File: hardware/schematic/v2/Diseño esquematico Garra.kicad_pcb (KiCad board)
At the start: 2 copper layers, 18 parts

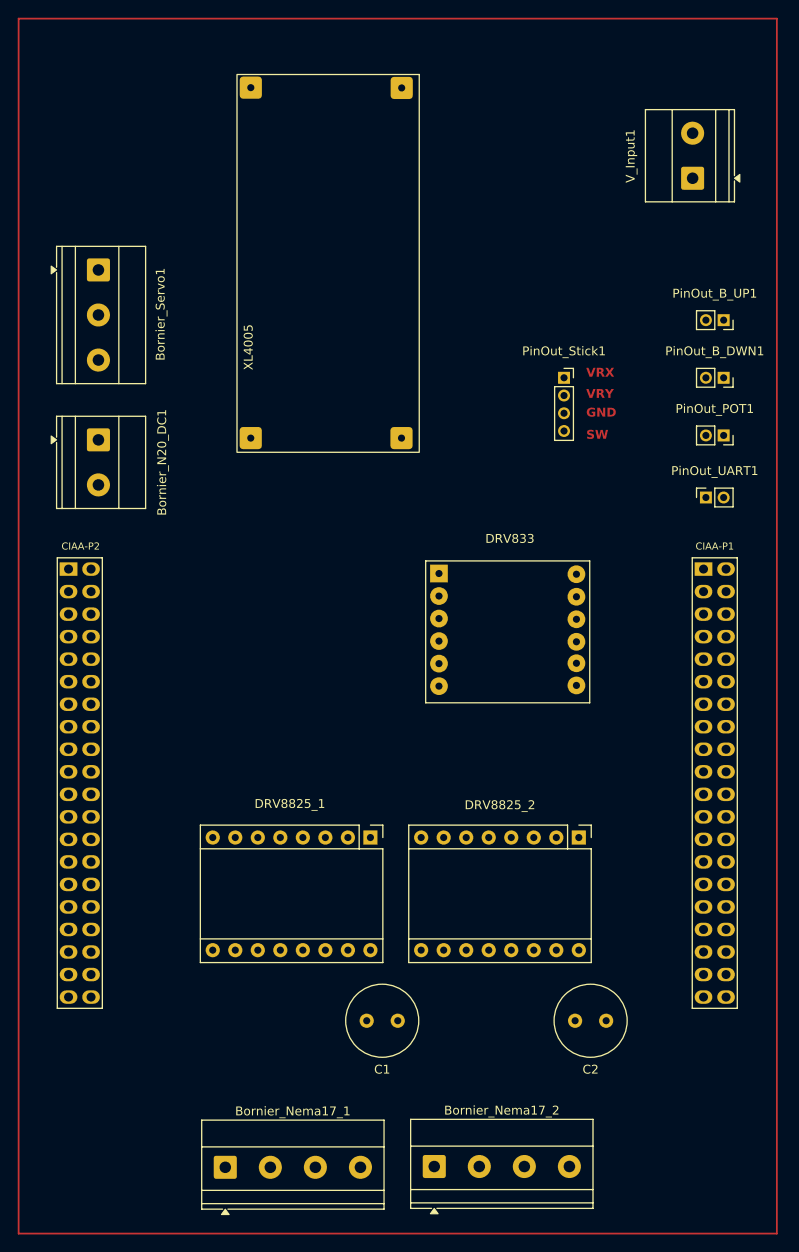
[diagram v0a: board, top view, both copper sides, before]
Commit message: feat: add PCB layout (#7)
* refactor

* feat: PCB routing first stage completed

* docs: Schematics PDF added

* fix: PCB border colision

* feat: Copper layers added to the PCB

* feat: New PCB design with new components [LED, B_M]

* feat: add through holes for connectivity & GNDs links

* feat: hole diameter adjustment

* fix: PDF

---------

Co-authored-by: ManuSavenia <saveniamanuel@egmail.com>
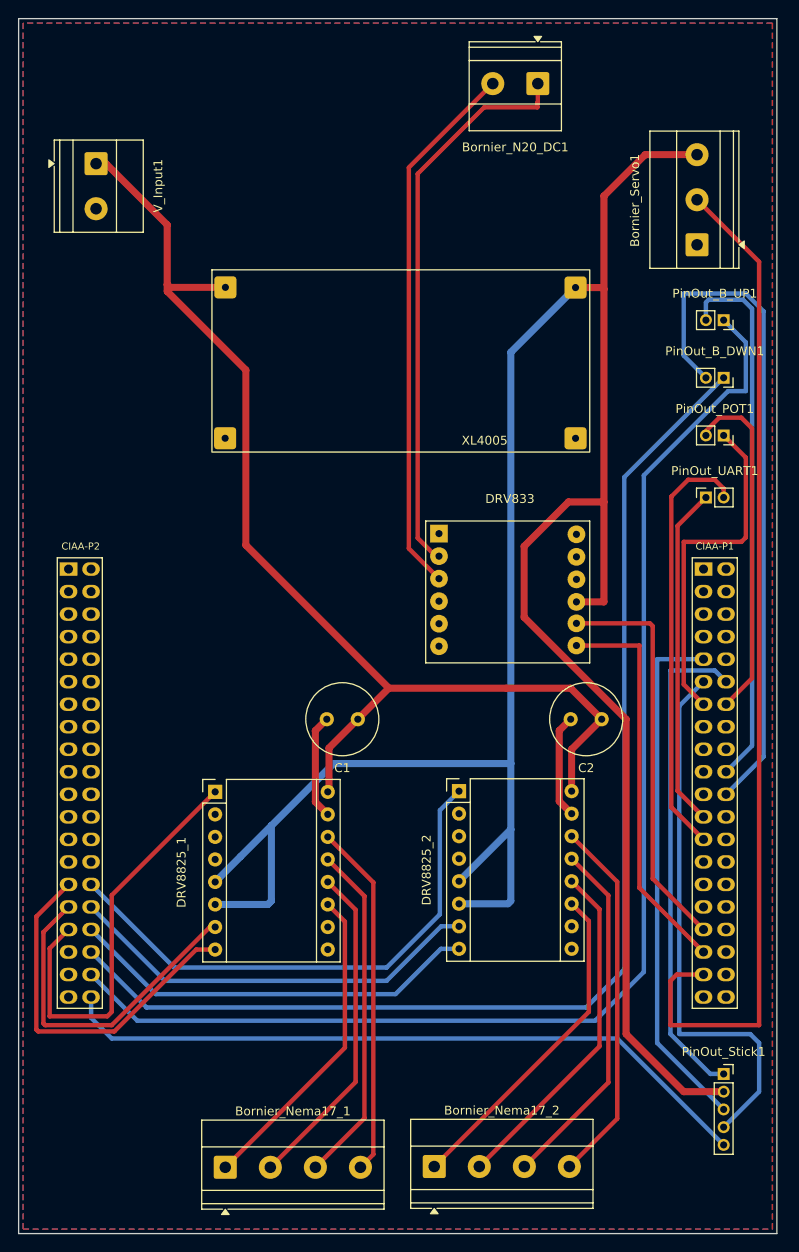
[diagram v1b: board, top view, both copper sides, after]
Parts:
- PinOut_Stick1: footprint Connector_PinSocket_2.00mm:PinSocket_1x04_P2.00mm_Vertical -> Connector_PinSocket_2.00mm:PinSocket_1x05_P2.00mm_Vertical
- moved PinOut_Stick1 80.5 mm to (114.5, 144.0)
- moved Bornier_Servo1 67.6 mm to (111.5, 50.5), turned to 90 degrees
- moved V_Input1 67.3 mm to (43.7, 41.4), turned to -90 degrees
- moved Bornier_N20_DC1 63.8 mm to (93.5, 32.3), turned to 180 degrees
- moved C1 34.3 mm to (73.2, 104.0)
- moved C2 34.0 mm to (100.8, 104.0)
- moved XL4005 32.1 mm to (56.8, 53.3), turned to 0 degrees
- moved DRV8825_1 18.3 mm to (57.2, 112.2), turned to 0 degrees
- moved DRV8825_2 14.5 mm to (84.7, 112.1), turned to 0 degrees
- moved DRV833 4.50 mm to (111.9, 99.2)
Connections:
- net TFIL2 renamed SERVO_PWM
- CIAA-P1 pad 33: IN1 -> IN2
- CIAA-P1 pad 35: IN2 -> IN1
- CIAA-P2 pad 36: unconnected-(CIAA-P2-GPIO5-Pad36) -> B_DWN
- CIAA-P2 pad 38: unconnected-(CIAA-P2-GPIO7-Pad38) -> B_UP
- CIAA-P2 pad 40: unconnected-(CIAA-P2-GPIO8-Pad40) -> SW
- PinOut_Stick1 pad 1: VRX -> GND_Stick
- PinOut_Stick1 pad 2: VRY -> 5V
- PinOut_Stick1 pad 3: GND_Stick -> VRX
- PinOut_Stick1 pad 4: SW -> VRY
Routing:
- net 5V: track 0.00 -> 289.4 mm
- net B_UP: track 0.00 -> 147.2 mm
- net B_DWN: track 0.00 -> 135.8 mm
- net 12V: track 0.00 -> 130.9 mm
- net SERVO_PWM: track 0.00 -> 115.0 mm
- net SW: track 0.00 -> 79.8 mm
- net GND_B_DWN: track 0.00 -> 76.6 mm
- net MOTOR_VCC: track 0.00 -> 63.7 mm
- net VRY: track 0.00 -> 61.4 mm
- net GND_B_UP: track 0.00 -> 61.2 mm
- net MOTOR_GND: track 0.00 -> 61.2 mm
- net EN2: track 0.00 -> 60.5 mm
- net VRX: track 0.00 -> 59.1 mm
- net GND_Stick: track 0.00 -> 55.7 mm
- net RS232_TX: track 0.00 -> 48.3 mm
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- added copper zone on B.Cu, net GND
- added copper zone on F.Cu, net GND
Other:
- board outline added: 85.5 x 137 mm
- board text removed: "GND"
- board text removed: "SW"
- board text removed: "VRX"
- board text removed: "VRY"
